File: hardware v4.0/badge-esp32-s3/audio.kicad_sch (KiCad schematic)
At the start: 4 parts, among them Q5 DTC114E

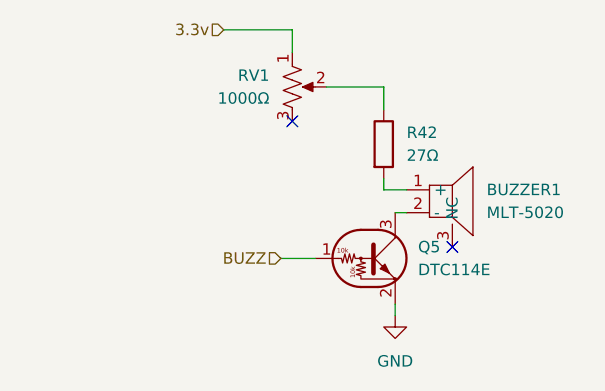
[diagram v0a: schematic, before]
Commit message: changed buzzer pot
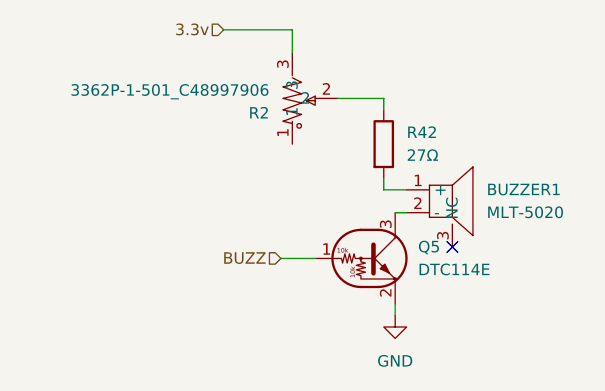
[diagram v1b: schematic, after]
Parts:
- removed RV1: 1000Ω, Potentiometer_THT:Potentiometer_Bourns_3296W_Vertical, symbol Device:R_Potentiometer_US
- added R2: 3362P-1-501_C48997906, lcsc-lib:RES-ADJ-TH_3362P, symbol lcsc-lib:3362P-1-501_C48997906
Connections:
- net 3.3v: now also R2.3
- net at R42.1: now also R2.2
- no-connect marks 2 -> 1
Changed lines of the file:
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@@
 		(at 171.45 99.06)
 	)
-	(no_connect
-		(at 153.67 85.09)
-	)
-	(wire
-		(pts
-			(xy 163.83 81.28) (xy 163.83 83.82)
-		)
-		(stroke
-			(width 0)
-			(type default)
-		)
-	)
 	(wire
 		(pts
@@
 	(wire
 		(pts
+			(xy 153.67 74.93) (xy 153.67 77.47)
+		)
+		(stroke
+			(width 0)
+			(type default)
+		)
+	)
+	(wire
+		(pts
 			(xy 163.83 92.71) (xy 166.37 92.71)
 		)
@@
 	(wire
 		(pts
-			(xy 153.67 74.93) (xy 153.67 77.47)
+			(xy 158.75 82.55) (xy 163.83 82.55)
 		)
 		(stroke
@@
 	(wire
 		(pts
-			(xy 157.48 81.28) (xy 163.83 81.28)
+			(xy 163.83 82.55) (xy 163.83 83.82)
 		)
 		(stroke
@@
 			)
 			(justify right)
+		)
+	)
+	(symbol
+		(lib_id "lcsc-lib:3362P-1-501_C48997906")
+		(at 156.21 82.55 270)
+		(mirror x)
+		(unit 1)
+		(exclude_from_sim no)
+		(in_bom yes)
+		(on_board yes)
+		(dnp no)
+		(property "Reference" "R2"
+			(at 151.13 84.2001 90)
+			(effects
+				(font
+					(size 1.27 1.27)
+				)
+				(justify right)
+			)
+		)
+		(property "Value" "3362P-1-501_C48997906"
+			(at 151.13 81.6601 90)
+			(effects
+				(font
+					(size 1.27 1.27)
+				)
+				(justify right)
+			)
+		)
+		(property "Footprint" "lcsc-lib:RES-ADJ-TH_3362P"
+			(at 146.05 82.55 0)
+			(effects
+				(font
+					(size 1.27 1.27)
+				)
+				(hide yes)
+			)
+		)
+		(property "Datasheet" "https://www.lcsc.com/datasheet/C48997906.pdf"
+			(at 143.51 82.55 0)
+			(effects
+				(font
+					(size 1.27 1.27)
+				)
+				(hide yes)
+			)
+		)
+		(property "Description" ""
+			(at 156.21 82.55 0)
+			(effects
+				(font
+					(size 1.27 1.27)
+				)
+				(hide yes)
+			)
+		)
+		(property "Manufacturer" "JIERR(捷而瑞)"
+			(at 140.97 82.55 0)
+			(effects
+				(font
+					(size 1.27 1.27)
+				)
+				(hide yes)
+			)
+		)
+		(property "MPN" "3362P-1-501"
+			(at 138.43 82.55 0)
+			(effects
+				(font
+					(size 1.27 1.27)
+				)
+				(hide yes)
+			)
+		)
+		(property "LCSC Part" "C48997906"
+			(at 135.89 82.55 0)
+			(effects
+				(font
+					(size 1.27 1.27)
+				)
+				(hide yes)
+			)
+		)
+		(pin "3"
+		)
+		(pin "1"
+		)
+		(pin "2"
+		)
+		(instances
+			(project ""
+				(path "/e2af9a6c-dbe9-4de2-9ba6-ea213a7300ec/df7bf792-82c5-4feb-b2e3-af668da9099d"
+					(reference "R2")
+					(unit 1)
+				)
+			)
 		)
 	)
@@
 					(unit 1)
 				)
-			)
-		)
-	)
-	(symbol
-		(lib_id "Device:R_Potentiometer_US")
-		(at 153.67 81.28 0)
-		(unit 1)
-		(exclude_from_sim no)
-		(in_bom yes)
-		(on_board yes)
-		(dnp no)
-		(fields_autoplaced yes)
-		(property "Reference" "RV1"
-			(at 151.13 80.0099 0)
-			(effects
-				(font
-					(size 1.27 1.27)
-				)
-				(justify right)
-			)
-		)
-		(property "Value" "1000Ω"
-			(at 151.13 82.5499 0)
-			(effects
-				(font
-					(size 1.27 1.27)
-				)
-				(justify right)
-			)
-		)
-		(property "Footprint" "Potentiometer_THT:Potentiometer_Bourns_3296W_Vertical"
-			(at 153.67 81.28 0)
-			(effects
-				(font
-					(size 1.27 1.27)
-				)
-				(hide yes)
-			)
-		)
-		(property "Datasheet" "https://item.szlcsc.com/datasheet/3296W-1-102LF/58119.html"
-			(at 153.67 81.28 0)
-			(effects
-				(font
-					(size 1.27 1.27)
-				)
-				(hide yes)
-			)
-		)
-		(property "Description" "Potentiometer, US symbol"
-			(at 153.67 81.28 0)
-			(effects
-				(font
-					(size 1.27 1.27)
-				)
-				(hide yes)
-			)
-		)
-		(property "LCSC" "C57089"
-			(at 153.67 81.28 0)
-			(effects
-				(font
-					(size 1.27 1.27)
-				)
-				(hide yes)
-			)
-		)
-		(property "FT Rotation Offset" "-90"
-			(at 153.67 81.28 0)
-			(effects
-				(font
-					(size 1.27 1.27)
-				)
-				(hide yes)
-			)
-		)
-		(pin "3"
-		)
-		(pin "1"
-		)
-		(pin "2"
-		)
-		(instances
-			(project ""
-				(path "/e2af9a6c-dbe9-4de2-9ba6-ea213a7300ec/df7bf792-82c5-4feb-b2e3-af668da9099d"
-					(reference "RV1")
-					(unit 1)
-				)
